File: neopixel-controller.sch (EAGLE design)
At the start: 8 parts, among them J1 Power, J2 AVR_SPI_PROG_3X2NS, U1 ATTiny85

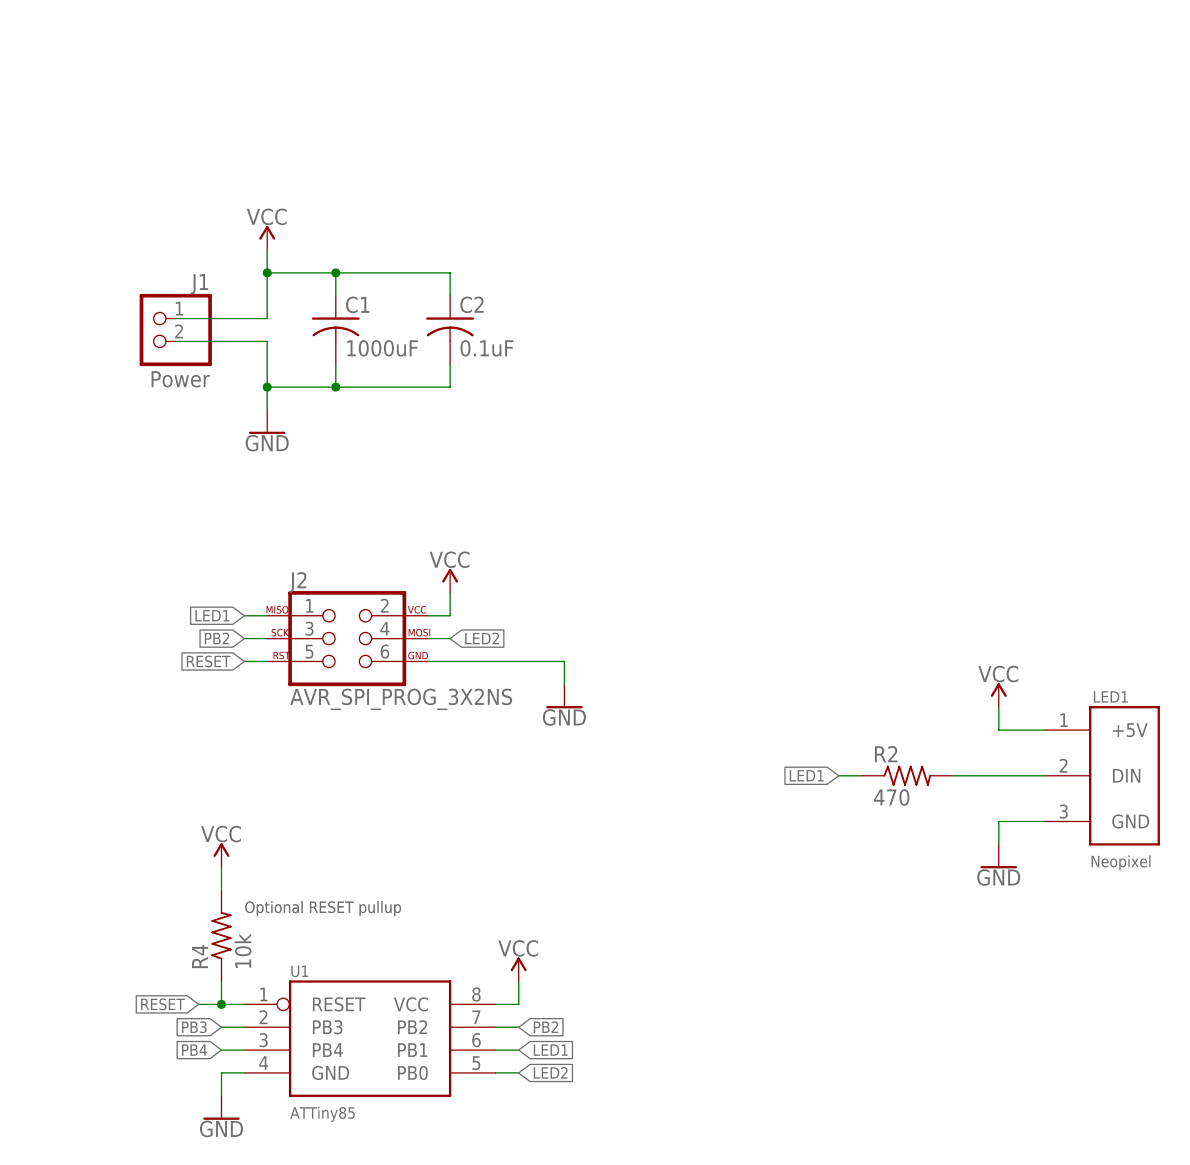
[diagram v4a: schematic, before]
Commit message: Revert neopixel-controller to neopixel-v1.0 and remove unnecessary things for 20th anniversary trophy production
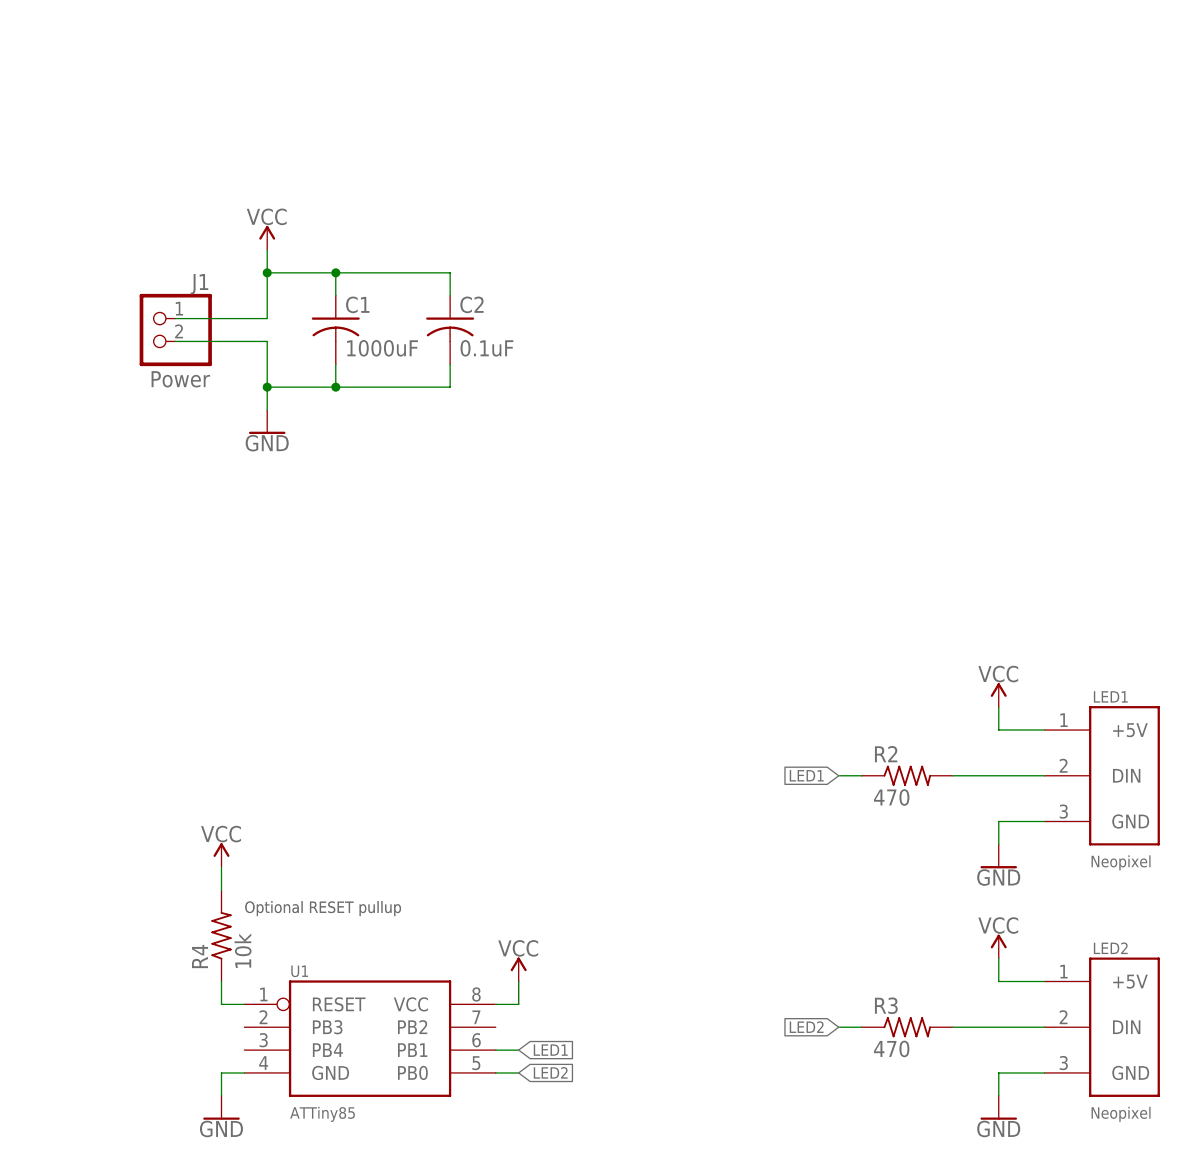
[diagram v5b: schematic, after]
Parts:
- removed J2: AVR_SPI_PROG_3X2NS, SparkFun-Connectors:AVR_SPI_PROG_3X2NS
- added LED2: Neopixel, JoshCustom:NEOPIXEL0.100_PINHEAD
- added R3: 470, resistor:R-US_R0805
- U1: device JoshCustom:ATTINY85SOIC8 -> JoshCustom:ATTINY85PDIP8_SOCKET
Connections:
- removed net PB2: J2.3, U1.PB2
- removed net PB3: U1.PB3
- removed net PB4: U1.PB4
- removed net RESET: J2.5, R4.1, U1.RESET
- new net N$1: LED2.DIN, R3.2
- new net N$5: R4.1, U1.RESET
- net GND: now also LED2.GND; no longer J2.6
- net LED1: no longer J2.1
- net LED2: now also R3.1; no longer J2.4
- net VCC: now also LED2.+5V; no longer J2.2
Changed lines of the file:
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@@
 <parts>
 <part name="J1" library="pinhead" library_urn="urn:adsk.eagle:library:325" deviceset="PINHD-1X2" device="" package3d_urn="urn:adsk.eagle:package:22435/2" value="Power"/>
-<part name="U1" library="JoshCustom" deviceset="ATTINY85" device="SOIC8" value="ATTiny85"/>
+<part name="U1" library="JoshCustom" deviceset="ATTINY85" device="PDIP8_SOCKET" value="ATTiny85"/>
 <part name="LED1" library="JoshCustom" deviceset="NEOPIXEL" device="0.100_PINHEAD" value="Neopixel"/>
+<part name="LED2" library="JoshCustom" deviceset="NEOPIXEL" device="0.100_PINHEAD" value="Neopixel"/>
 <part name="R2" library="resistor" library_urn="urn:adsk.eagle:library:348" deviceset="R-US_" device="R0805" package3d_urn="urn:adsk.eagle:package:26059/1" value="470"/>
+<part name="R3" library="resistor" library_urn="urn:adsk.eagle:library:348" deviceset="R-US_" device="R0805" package3d_urn="urn:adsk.eagle:package:26059/1" value="470"/>
 <part name="R4" library="resistor" library_urn="urn:adsk.eagle:library:348" deviceset="R-US_" device="R0805" package3d_urn="urn:adsk.eagle:package:26059/1" value="10k"/>
 <part name="SUPPLY1" library="SparkFun-PowerSymbols" deviceset="VCC" device=""/>
 <part name="SUPPLY2" library="SparkFun-PowerSymbols" deviceset="VCC" device=""/>
+<part name="SUPPLY3" library="SparkFun-PowerSymbols" deviceset="VCC" device=""/>
 <part name="SUPPLY4" library="SparkFun-PowerSymbols" deviceset="VCC" device=""/>
 <part name="GND1" library="SparkFun-PowerSymbols" deviceset="GND" device=""/>
 <part name="GND2" library="SparkFun-PowerSymbols" deviceset="GND" device=""/>
 <part name="GND3" library="SparkFun-PowerSymbols" deviceset="GND" device=""/>
+<part name="GND4" library="SparkFun-PowerSymbols" deviceset="GND" device=""/>
 <part name="SUPPLY5" library="SparkFun-PowerSymbols" deviceset="VCC" device=""/>
 <part name="C2" library="resistor" library_urn="urn:adsk.eagle:library:348" deviceset="C-US" device="C0805" package3d_urn="urn:adsk.eagle:package:23617/2" value="0.1uF"/>
 <part name="C1" library="JoshCustom" deviceset="CAPACITOR" device="" value="1000uF"/>
-<part name="J2" library="SparkFun-Connectors" deviceset="AVR_SPI_PROG_3X2" device="NS"/>
-<part name="SUPPLY6" library="SparkFun-PowerSymbols" deviceset="VCC" device=""/>
-<part name="GND7" library="SparkFun-PowerSymbols" deviceset="GND" device=""/>
 </parts>
 <sheets>
@@
 <attribute name="VALUE" x="109.22" y="30.48" size="1.27" layer="96"/>
 </instance>
+<instance part="LED2" gate="G$1" x="109.22" y="5.08" smashed="yes">
+<attribute name="NAME" x="109.474" y="20.828" size="1.27" layer="95"/>
+<attribute name="VALUE" x="109.22" y="2.54" size="1.27" layer="96"/>
+</instance>
 <instance part="R2" gate="G$1" x="88.9" y="40.64" smashed="yes">
 <attribute name="NAME" x="85.09" y="42.1386" size="1.778" layer="95"/>
 <attribute name="VALUE" x="85.09" y="37.338" size="1.778" layer="96"/>
 </instance>
+<instance part="R3" gate="G$1" x="88.9" y="12.7" smashed="yes">
+<attribute name="NAME" x="85.09" y="14.1986" size="1.778" layer="95"/>
+<attribute name="VALUE" x="85.09" y="9.398" size="1.778" layer="96"/>
+</instance>
 <instance part="R4" gate="G$1" x="12.7" y="22.86" smashed="yes" rot="R90">
 <attribute name="NAME" x="11.2014" y="19.05" size="1.778" layer="95" rot="R90"/>
@@
 <attribute name="VALUE" x="45.72" y="20.574" size="1.778" layer="96" align="bottom-center"/>
 </instance>
+<instance part="SUPPLY3" gate="G$1" x="99.06" y="20.32" smashed="yes">
+<attribute name="VALUE" x="99.06" y="23.114" size="1.778" layer="96" align="bottom-center"/>
+</instance>
 <instance part="SUPPLY4" gate="G$1" x="99.06" y="48.26" smashed="yes">
 <attribute name="VALUE" x="99.06" y="51.054" size="1.778" layer="96" align="bottom-center"/>
@@
 <instance part="GND3" gate="1" x="99.06" y="30.48" smashed="yes">
 <attribute name="VALUE" x="99.06" y="30.226" size="1.778" layer="96" align="top-center"/>
+</instance>
+<instance part="GND4" gate="1" x="99.06" y="2.54" smashed="yes">
+<attribute name="VALUE" x="99.06" y="2.286" size="1.778" layer="96" align="top-center"/>
 </instance>
 <instance part="SUPPLY5" gate="G$1" x="12.7" y="30.48" smashed="yes">
@@
 <attribute name="NAME" x="26.416" y="92.075" size="1.778" layer="95"/>
 <attribute name="VALUE" x="26.416" y="87.249" size="1.778" layer="96"/>
-</instance>
-<instance part="J2" gate="G$1" x="25.4" y="55.88" smashed="yes">
-<attribute name="NAME" x="20.32" y="61.468" size="1.778" layer="95" font="vector"/>
-<attribute name="VALUE" x="20.32" y="48.514" size="1.778" layer="96" font="vector"/>
-</instance>
-<instance part="SUPPLY6" gate="G$1" x="38.1" y="60.96" smashed="yes">
-<attribute name="VALUE" x="38.1" y="63.754" size="1.778" layer="96" align="bottom-center"/>
-</instance>
-<instance part="GND7" gate="1" x="50.8" y="48.26" smashed="yes">
-<attribute name="VALUE" x="50.8" y="48.006" size="1.778" layer="96" align="top-center"/>
 </instance>
 </instances>
@@
 </segment>
 <segment>
+<pinref part="LED2" gate="G$1" pin="+5V"/>
+<wire x1="104.14" y1="17.78" x2="99.06" y2="17.78" width="0.1524" layer="91"/>
+<pinref part="SUPPLY3" gate="G$1" pin="VCC"/>
+<wire x1="99.06" y1="17.78" x2="99.06" y2="20.32" width="0.1524" layer="91"/>
+</segment>
+<segment>
 <pinref part="LED1" gate="G$1" pin="+5V"/>
 <wire x1="104.14" y1="45.72" x2="99.06" y2="45.72" width="0.1524" layer="91"/>
@@
 <pinref part="SUPPLY5" gate="G$1" pin="VCC"/>
 <wire x1="12.7" y1="27.94" x2="12.7" y2="30.48" width="0.1524" layer="91"/>
-</segment>
-<segment>
-<pinref part="J2" gate="G$1" pin="2"/>
-<pinref part="SUPPLY6" gate="G$1" pin="VCC"/>
-<wire x1="35.56" y1="58.42" x2="38.1" y2="58.42" width="0.1524" layer="91"/>
-<wire x1="38.1" y1="58.42" x2="38.1" y2="60.96" width="0.1524" layer="91"/>
 </segment>
 </net>
@@
 </segment>
 <segment>
+<pinref part="GND4" gate="1" pin="GND"/>
+<wire x1="99.06" y1="5.08" x2="99.06" y2="7.62" width="0.1524" layer="91"/>
+<pinref part="LED2" gate="G$1" pin="GND"/>
+<wire x1="99.06" y1="7.62" x2="104.14" y2="7.62" width="0.1524" layer="91"/>
+</segment>
+<segment>
 <pinref part="GND3" gate="1" pin="GND"/>
 <wire x1="99.06" y1="33.02" x2="99.06" y2="35.56" width="0.1524" layer="91"/>
@@
 <wire x1="99.06" y1="35.56" x2="104.14" y2="35.56" width="0.1524" layer="91"/>
 </segment>
-<segment>
-<pinref part="J2" gate="G$1" pin="6"/>
-<wire x1="35.56" y1="53.34" x2="50.8" y2="53.34" width="0.1524" layer="91"/>
-<pinref part="GND7" gate="1" pin="GND"/>
-<wire x1="50.8" y1="53.34" x2="50.8" y2="50.8" width="0.1524" layer="91"/>
+</net>
+<net name="N$5" class="0">
+<segment>
+<pinref part="U1" gate="G$1" pin="RESET"/>
+<wire x1="15.24" y1="15.24" x2="12.7" y2="15.24" width="0.1524" layer="91"/>
+<pinref part="R4" gate="G$1" pin="1"/>
+<wire x1="12.7" y1="15.24" x2="12.7" y2="17.78" width="0.1524" layer="91"/>
+</segment>
+</net>
+<net name="N$1" class="0">
+<segment>
+<pinref part="LED2" gate="G$1" pin="DIN"/>
+<pinref part="R3" gate="G$1" pin="2"/>
+<wire x1="104.14" y1="12.7" x2="93.98" y2="12.7" width="0.1524" layer="91"/>
 </segment>
 </net>
@@
 </segment>
 </net>
-<net name="PB3" class="0">
-<segment>
-<pinref part="U1" gate="G$1" pin="PB3"/>
-<wire x1="15.24" y1="12.7" x2="12.7" y2="12.7" width="0.1524" layer="91"/>
-<label x="12.7" y="12.7" size="1.27" layer="95" rot="R180" xref="yes"/>
-</segment>
-</net>
-<net name="PB4" class="0">
-<segment>
-<pinref part="U1" gate="G$1" pin="PB4"/>
-<wire x1="15.24" y1="10.16" x2="12.7" y2="10.16" width="0.1524" layer="91"/>
-<label x="12.7" y="10.16" size="1.27" layer="95" rot="R180" xref="yes"/>
-</segment>
-</net>
-<net name="PB2" class="0">
-<segment>
-<pinref part="U1" gate="G$1" pin="PB2"/>
-<wire x1="43.18" y1="12.7" x2="45.72" y2="12.7" width="0.1524" layer="91"/>
-<label x="45.72" y="12.7" size="1.27" layer="95" xref="yes"/>
-</segment>
-<segment>
-<pinref part="J2" gate="G$1" pin="3"/>
-<wire x1="17.78" y1="55.88" x2="15.24" y2="55.88" width="0.1524" layer="91"/>
-<label x="15.24" y="55.88" size="1.27" layer="95" rot="R180" xref="yes"/>
-</segment>
-</net>
 <net name="LED2" class="0">
 <segment>
@@
 </segment>
 <segment>
-<pinref part="J2" gate="G$1" pin="4"/>
-<wire x1="35.56" y1="55.88" x2="38.1" y2="55.88" width="0.1524" layer="91"/>
-<label x="38.1" y="55.88" size="1.27" layer="95" xref="yes"/>
+<pinref part="R3" gate="G$1" pin="1"/>
+<wire x1="83.82" y1="12.7" x2="81.28" y2="12.7" width="0.1524" layer="91"/>
+<label x="81.28" y="12.7" size="1.27" layer="95" rot="R180" xref="yes"/>
 </segment>
 </net>
@@
 <label x="81.28" y="40.64" size="1.27" layer="95" rot="R180" xref="yes"/>
 </segment>
-<segment>
-<pinref part="J2" gate="G$1" pin="1"/>
-<wire x1="17.78" y1="58.42" x2="15.24" y2="58.42" width="0.1524" layer="91"/>
-<label x="15.24" y="58.42" size="1.27" layer="95" rot="R180" xref="yes"/>
-</segment>
-</net>
-<net name="RESET" class="0">
-<segment>
-<pinref part="J2" gate="G$1" pin="5"/>
-<wire x1="17.78" y1="53.34" x2="15.24" y2="53.34" width="0.1524" layer="91"/>
-<label x="15.24" y="53.34" size="1.27" layer="95" rot="R180" xref="yes"/>
-</segment>
-<segment>
-<pinref part="U1" gate="G$1" pin="RESET"/>
-<wire x1="15.24" y1="15.24" x2="12.7" y2="15.24" width="0.1524" layer="91"/>
-<label x="10.16" y="15.24" size="1.27" layer="95" rot="R180" xref="yes"/>
-<pinref part="R4" gate="G$1" pin="1"/>
-<wire x1="12.7" y1="15.24" x2="10.16" y2="15.24" width="0.1524" layer="91"/>
-<wire x1="12.7" y1="17.78" x2="12.7" y2="15.24" width="0.1524" layer="91"/>
-<junction x="12.7" y="15.24"/>
-</segment>
-</net>
+</net>

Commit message: Reroute original controller to use a SOIC ATtiny85
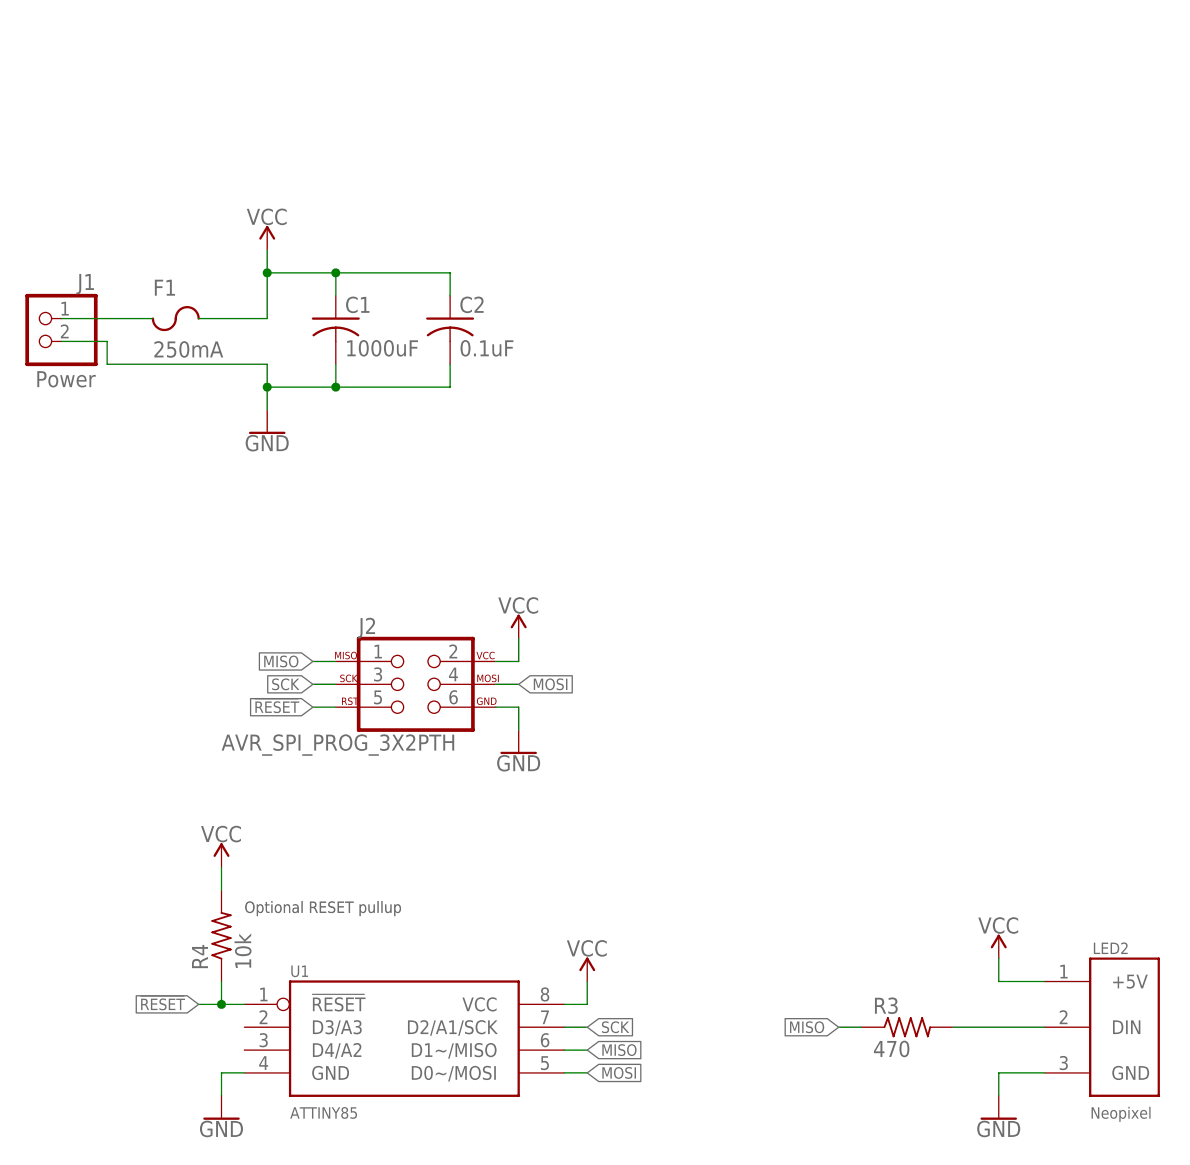
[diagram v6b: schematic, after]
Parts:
- removed LED1: Neopixel, JoshCustom:NEOPIXEL0.100_PINHEAD
- removed R2: 470, resistor:R-US_R0805
- added F1: 250mA, JoshCustom:FUSE
- added J2: AVR_SPI_PROG_3X2PTH, SparkFun-Connectors:AVR_SPI_PROG_3X2PTH
- U1: value ATTiny85 -> ATTINY85; device JoshCustom:ATTINY85PDIP8_SOCKET -> JoshCustom:ATTINY85
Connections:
- removed net LED1: R2.1, U1.PB1
- removed net LED2: R3.1, U1.PB0
- removed net N$5: R4.1, U1.RESET
- new net !RESET!: J2.5, R4.1, U1.!RESET!
- new net MISO: J2.1, R3.1, U1.D1~/MISO
- new net MOSI: J2.4, U1.D0~/MOSI
- new net SCK: J2.3, U1.D2/A1/SCK
- net GND: now also J2.6; no longer LED1.GND
- net N$2: now also F1.1, J1.1; no longer LED1.DIN, R2.2
- net VCC: now also F1.2, J2.2; no longer J1.1, LED1.+5V
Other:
- moved on the sheet: J1, U1
